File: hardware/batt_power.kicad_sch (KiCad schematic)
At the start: 11 parts, among them J5 JST_PH_01x03, J6 Conn_01x01, J8 Conn_01x01, Q1 AO3400A, U6 TPS7A2030PDBV

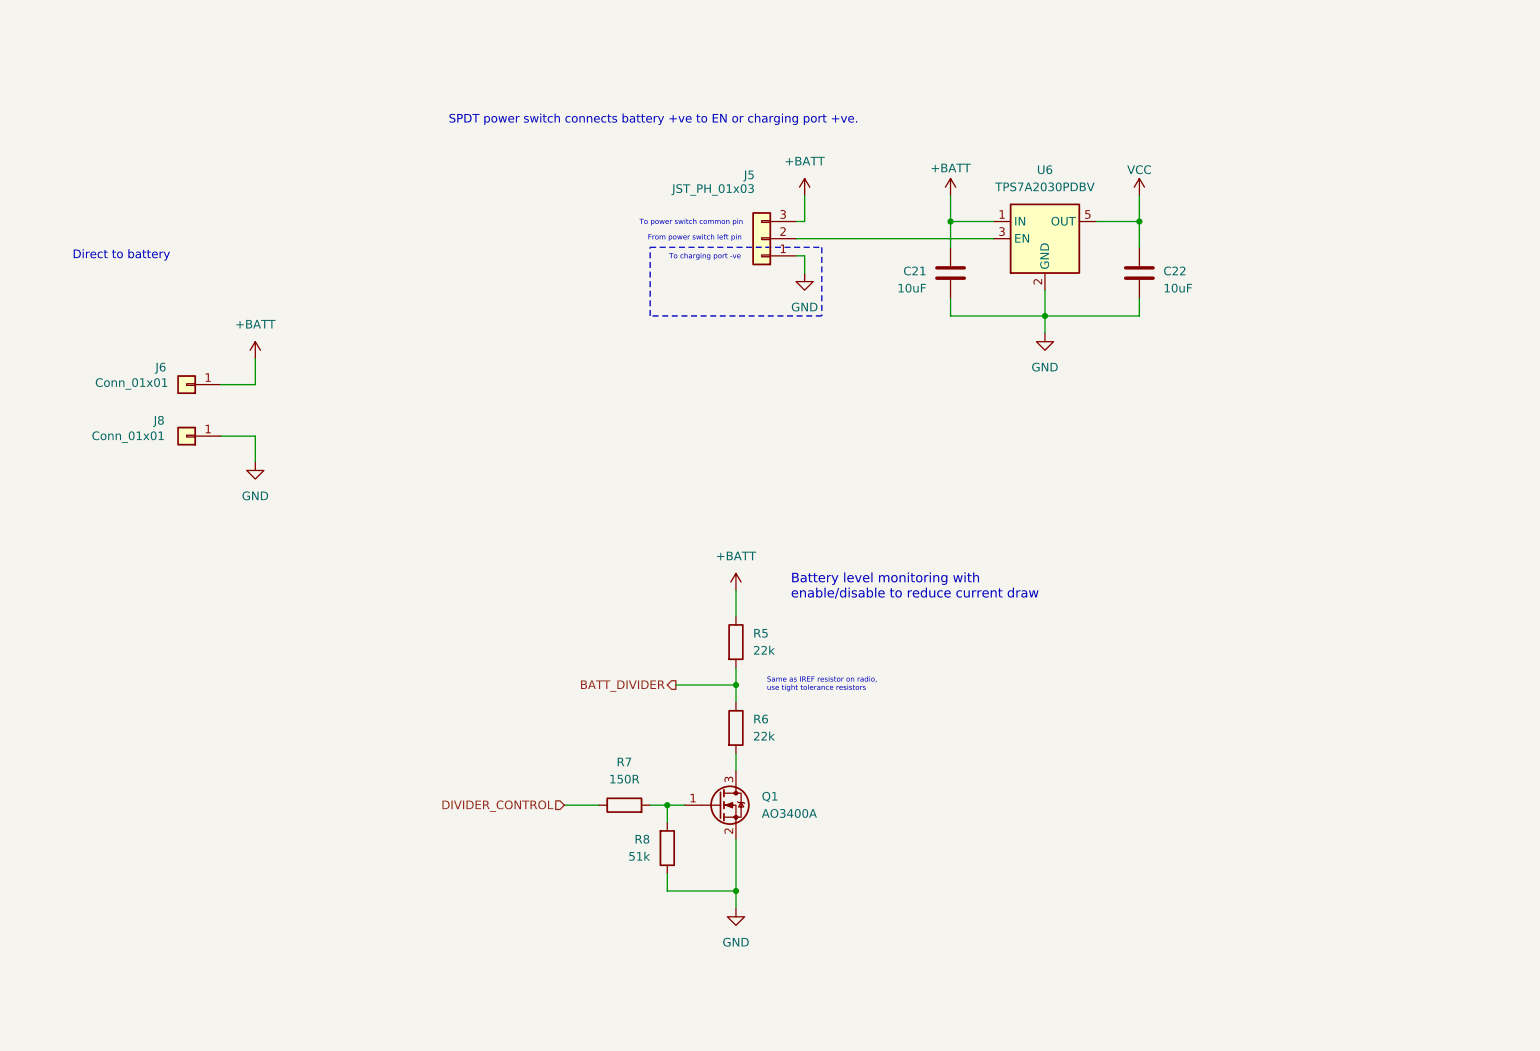
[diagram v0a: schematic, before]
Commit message: Added separate LDO for NRF24
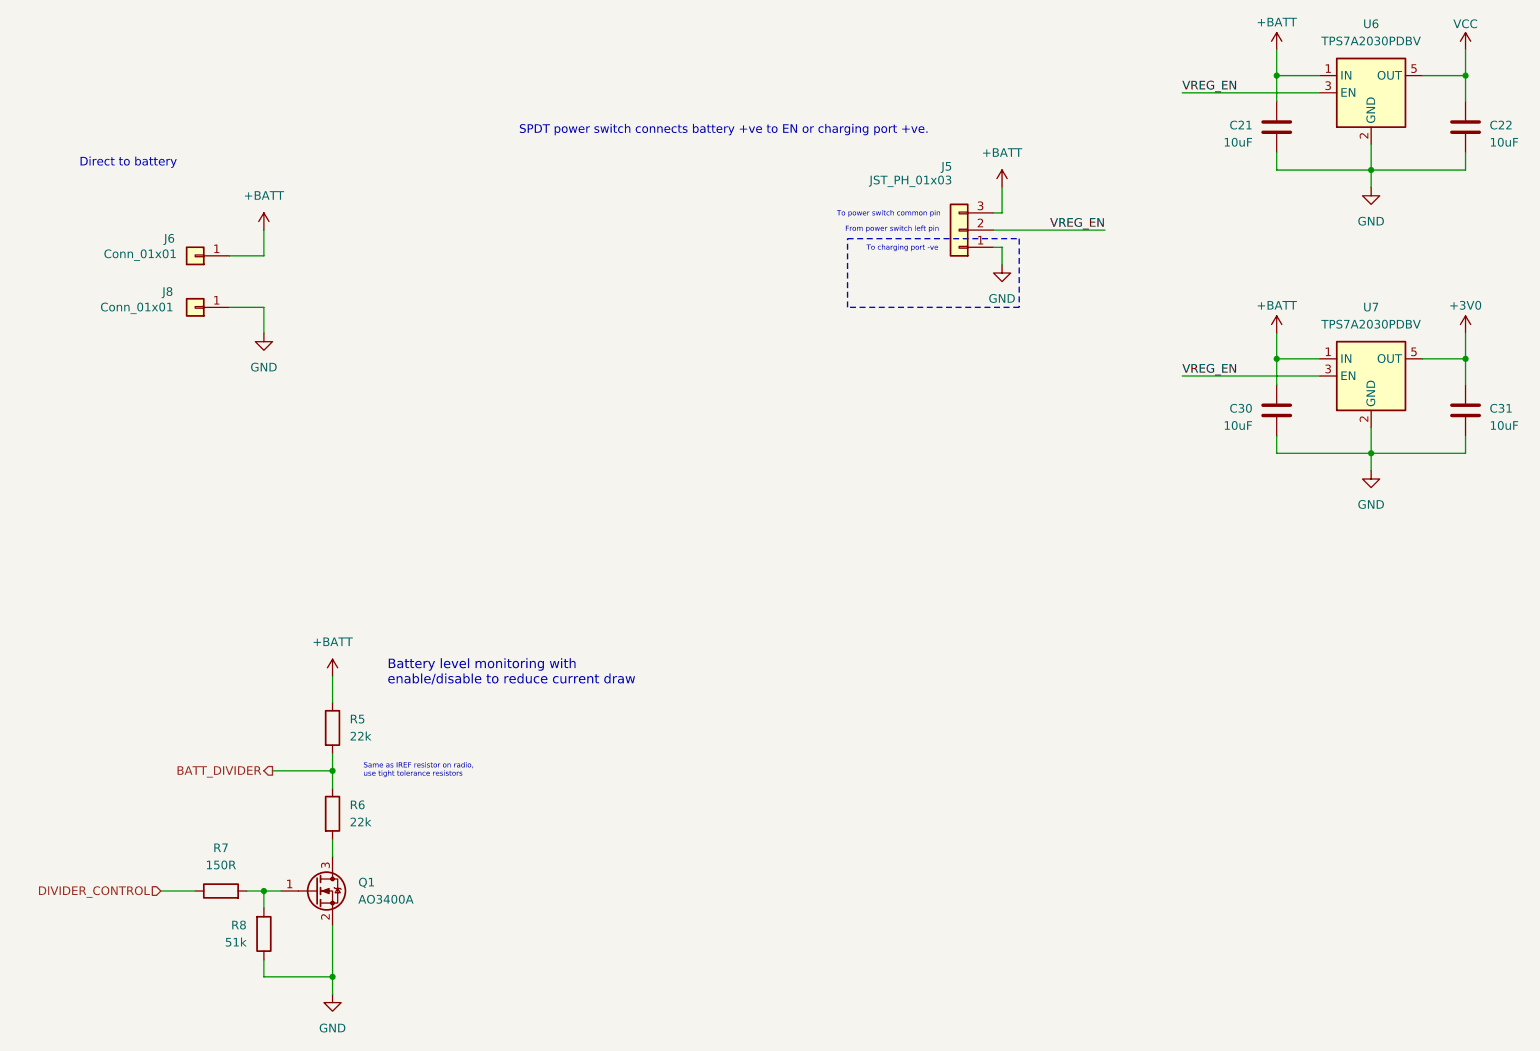
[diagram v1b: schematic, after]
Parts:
- added C30, C31: 10uF, Capacitor_SMD:C_0603_1608Metric_Pad1.08x0.95mm_HandSolder, symbol Device:C
- added U7: TPS7A2030PDBV, Package_TO_SOT_SMD:SOT-23-5_HandSoldering, symbol heli_symbols:TPS7A20
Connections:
- net +BATT: now also C30.1, U7.1 (IN)
- net GND: now also C30.2, C31.2, U7.2 (GND)
- net VREG_EN: now reaches J5.2 (Pin_2), U6.3 (EN)
- net VREG_EN: now also U7.3 (EN)
- new net +3V0: C31.1, U7.5 (OUT)
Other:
- moved on the sheet: C21, C22, J5, J6, J8, Q1, R5, R6, R7, R8, U6

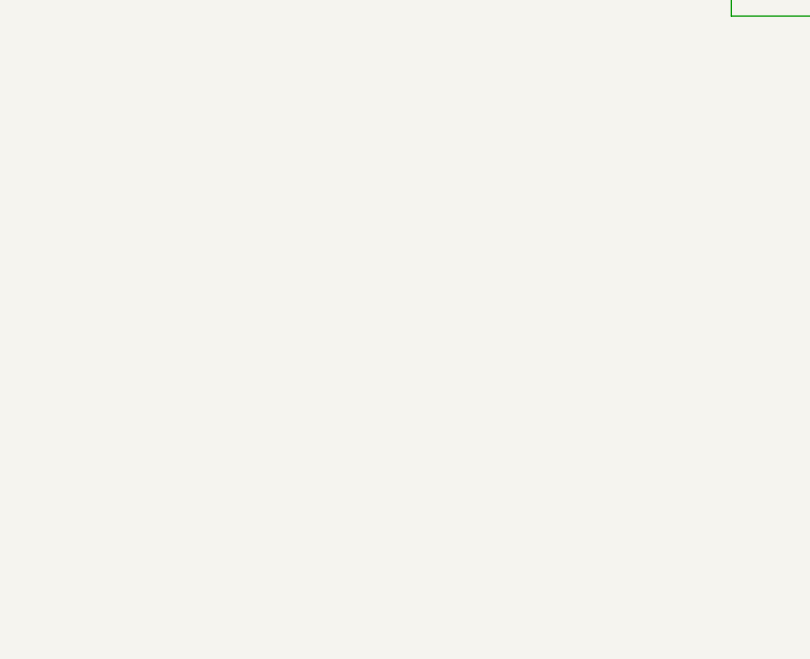
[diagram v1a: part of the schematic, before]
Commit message: Added power testpoints
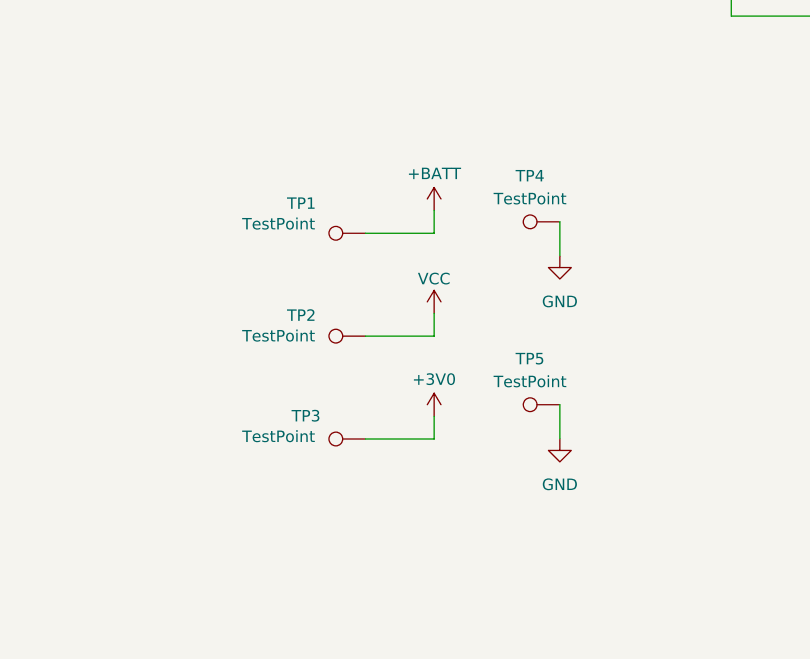
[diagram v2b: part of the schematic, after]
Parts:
- added TP1, TP2, TP3: TestPoint, TestPoint:TestPoint_Pad_1.5x1.5mm, symbol Connector:TestPoint
- added TP4: TestPoint, TestPoint:TestPoint_Pad_D1.5mm, symbol Connector:TestPoint
- added TP5: TestPoint, TestPoint:TestPoint_Keystone_5019_Minature, symbol Connector:TestPoint
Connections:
- net +3V0: now also TP3.1
- net +BATT: now also TP1.1
- net GND: now also TP4.1, TP5.1
- net VCC: now also TP2.1

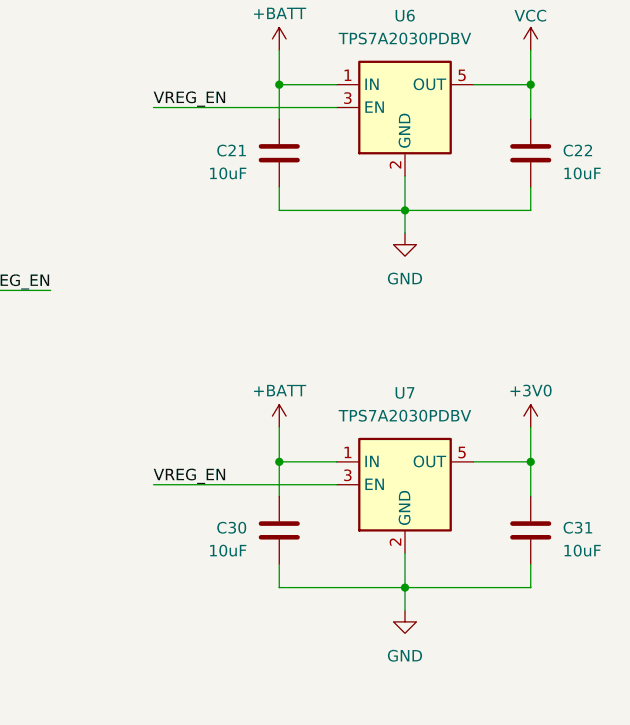
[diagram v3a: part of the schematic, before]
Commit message: Updated VRM capacitor values
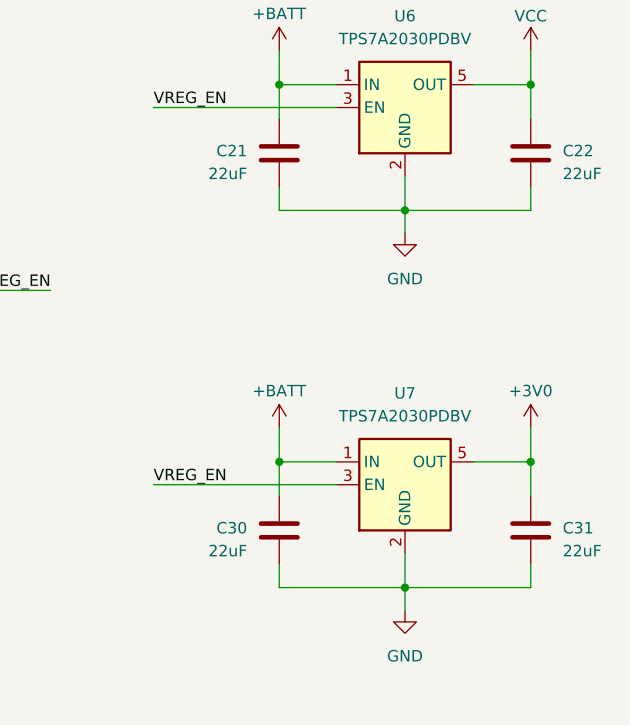
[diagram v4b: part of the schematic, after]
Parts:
- C21, C22, C30, C31: value 10uF -> 22uF
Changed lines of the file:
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@@
 			)
 		)
-		(property "Value" "10uF"
+		(property "Value" "22uF"
 			(at 243.586 44.196 0)
 			(effects
@@
 			)
 		)
-		(property "Value" "10uF"
+		(property "Value" "22uF"
 			(at 243.586 86.106 0)
 			(effects
@@
 			)
 		)
-		(property "Value" "10uF"
+		(property "Value" "22uF"
 			(at 208.534 86.106 0)
 			(effects
@@
 			)
 		)
-		(property "Value" "10uF"
+		(property "Value" "22uF"
 			(at 208.534 44.196 0)
 			(effects

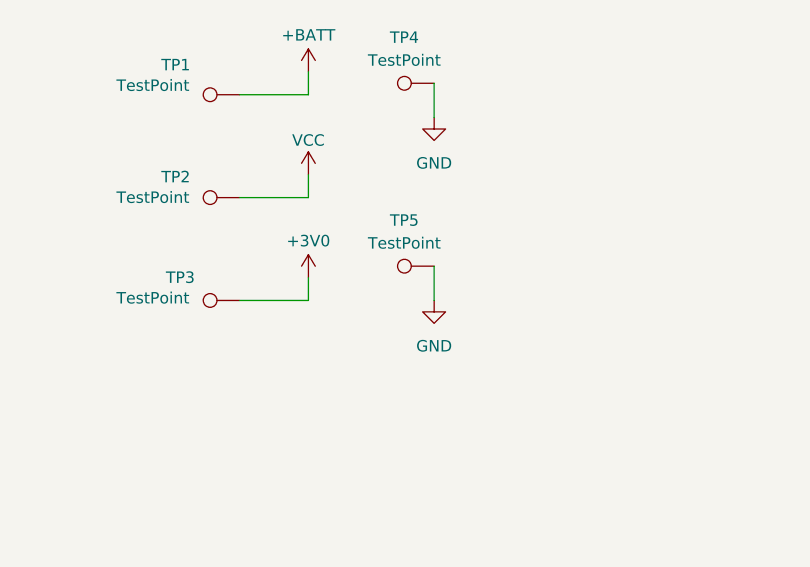
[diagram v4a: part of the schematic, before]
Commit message: Shifted radio components and testpoints around
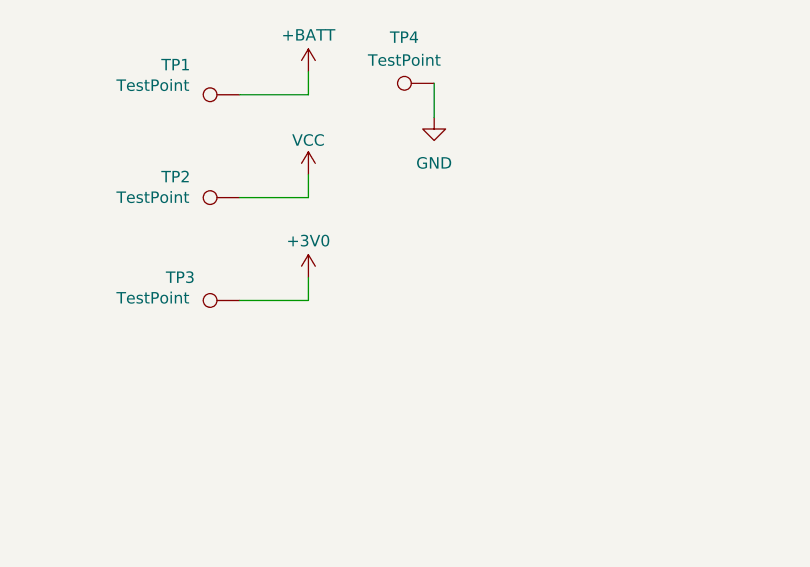
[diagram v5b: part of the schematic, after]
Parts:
- removed TP5: TestPoint, TestPoint:TestPoint_Keystone_5019_Minature, symbol Connector:TestPoint
- TP2: footprint TestPoint:TestPoint_Pad_1.5x1.5mm -> TestPoint:TestPoint_Pad_D1.5mm
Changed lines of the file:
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@@
-	(wire
-		(pts
-			(xy 193.04 133.35) (xy 193.04 137.16)
-		)
-		(stroke
-			(width 0)
-			(type default)
-		)
-	)
 	(wire
 		(pts
@@
 	)
 	(symbol
-		(lib_id "Connector:TestPoint")
-		(at 193.04 133.35 90)
-		(unit 1)
-		(exclude_from_sim no)
-		(in_bom yes)
-		(on_board yes)
-		(dnp no)
-		(fields_autoplaced yes)
-		(property "Reference" "TP5"
-			(at 189.738 128.27 90)
-			(effects
-				(font
-					(size 1.27 1.27)
-				)
-			)
-		)
-		(property "Value" "TestPoint"
-			(at 189.738 130.81 90)
-			(effects
-				(font
-					(size 1.27 1.27)
-				)
-			)
-		)
-		(property "Footprint" "TestPoint:TestPoint_Keystone_5019_Minature"
-			(at 193.04 128.27 0)
-			(effects
-				(font
-					(size 1.27 1.27)
-				)
-				(hide yes)
-			)
-		)
-		(property "Datasheet" "~"
-			(at 193.04 128.27 0)
-			(effects
-				(font
-					(size 1.27 1.27)
-				)
-				(hide yes)
-			)
-		)
-		(property "Description" "test point"
-			(at 193.04 133.35 0)
-			(effects
-				(font
-					(size 1.27 1.27)
-				)
-				(hide yes)
-			)
-		)
-		(pin "1"
-		)
-		(instances
-			(project "heli_avionics"
-				(path "/c384ea46-0dfb-4673-b2f4-1f88fafbcaa5/f8f87cfe-571f-4a92-acee-79776e4ce004"
-					(reference "TP5")
-					(unit 1)
-				)
-			)
-		)
-	)
-	(symbol
 		(lib_id "power:GND")
 		(at 226.06 50.8 0)
@@
 	)
 	(symbol
-		(lib_id "power:GND")
-		(at 193.04 137.16 0)
-		(unit 1)
-		(exclude_from_sim no)
-		(in_bom yes)
-		(on_board yes)
-		(dnp no)
-		(fields_autoplaced yes)
-		(property "Reference" "#PWR062"
-			(at 193.04 143.51 0)
-			(effects
-				(font
-					(size 1.27 1.27)
-				)
-				(hide yes)
-			)
-		)
-		(property "Value" "GND"
-			(at 193.04 142.24 0)
-			(effects
-				(font
-					(size 1.27 1.27)
-				)
-			)
-		)
-		(property "Footprint" ""
-			(at 193.04 137.16 0)
-			(effects
-				(font
-					(size 1.27 1.27)
-				)
-				(hide yes)
-			)
-		)
-		(property "Datasheet" ""
-			(at 193.04 137.16 0)
-			(effects
-				(font
-					(size 1.27 1.27)
-				)
-				(hide yes)
-			)
-		)
-		(property "Description" "Power symbol creates a global label with name \"GND\" , ground"
-			(at 193.04 137.16 0)
-			(effects
-				(font
-					(size 1.27 1.27)
-				)
-				(hide yes)
-			)
-		)
-		(pin "1"
-		)
-		(instances
-			(project "heli_avionics"
-				(path "/c384ea46-0dfb-4673-b2f4-1f88fafbcaa5/f8f87cfe-571f-4a92-acee-79776e4ce004"
-					(reference "#PWR062")
-					(unit 1)
-				)
-			)
-		)
-	)
-	(symbol
 		(lib_id "Device:R")
 		(at 55.88 154.94 90)
@@
 			)
 		)
-		(property "Footprint" "TestPoint:TestPoint_Pad_1.5x1.5mm"
+		(property "Footprint" "TestPoint:TestPoint_Pad_D1.5mm"
 			(at 171.45 120.65 0)
 			(effects

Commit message: Fixed ERC errors
Had to exclude warning for connecting ground to the bidirectional SA0 pin (pin 5) on the pressure sensor.
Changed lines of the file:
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@@
+	)
+	(junction
+		(at 62.23 60.96)
+		(diameter 0)
+		(color 0 0 0 0)
+	)
+	(junction
+		(at 62.23 68.58)
+		(diameter 0)
+		(color 0 0 0 0)
 	)
 	(junction
@@
 	(wire
 		(pts
+			(xy 62.23 68.58) (xy 72.39 68.58)
+		)
+		(stroke
+			(width 0)
+			(type default)
+		)
+	)
+	(wire
+		(pts
 			(xy 72.39 160.02) (xy 72.39 167.64)
 		)
@@
 	(wire
 		(pts
+			(xy 62.23 68.58) (xy 62.23 72.39)
+		)
+		(stroke
+			(width 0)
+			(type default)
+		)
+	)
+	(wire
+		(pts
 			(xy 212.09 45.72) (xy 212.09 48.26)
 		)
@@
 	(wire
 		(pts
+			(xy 72.39 60.96) (xy 62.23 60.96)
+		)
+		(stroke
+			(width 0)
+			(type default)
+		)
+	)
+	(wire
+		(pts
 			(xy 226.06 86.36) (xy 226.06 90.17)
 		)
@@
 	(wire
 		(pts
+			(xy 72.39 57.15) (xy 72.39 60.96)
+		)
+		(stroke
+			(width 0)
+			(type default)
+		)
+	)
+	(wire
+		(pts
 			(xy 62.23 165.1) (xy 62.23 167.64)
 		)
@@
 	(wire
 		(pts
-			(xy 62.23 68.58) (xy 62.23 72.39)
-		)
-		(stroke
-			(width 0)
-			(type default)
-		)
-	)
-	(wire
-		(pts
 			(xy 212.09 30.48) (xy 212.09 34.29)
 		)
@@
 		(pts
 			(xy 212.09 34.29) (xy 218.44 34.29)
+		)
+		(stroke
+			(width 0)
+			(type default)
+		)
+	)
+	(wire
+		(pts
+			(xy 72.39 68.58) (xy 72.39 72.39)
 		)
 		(stroke
@@
 	)
 	(symbol
+		(lib_id "power:PWR_FLAG")
+		(at 72.39 72.39 180)
+		(unit 1)
+		(exclude_from_sim no)
+		(in_bom yes)
+		(on_board yes)
+		(dnp no)
+		(fields_autoplaced yes)
+		(property "Reference" "#FLG02"
+			(at 72.39 74.295 0)
+			(effects
+				(font
+					(size 1.27 1.27)
+				)
+				(hide yes)
+			)
+		)
+		(property "Value" "PWR_FLAG"
+			(at 72.39 77.47 0)
+			(effects
+				(font
+					(size 1.27 1.27)
+				)
+			)
+		)
+		(property "Footprint" ""
+			(at 72.39 72.39 0)
+			(effects
+				(font
+					(size 1.27 1.27)
+				)
+				(hide yes)
+			)
+		)
+		(property "Datasheet" "~"
+			(at 72.39 72.39 0)
+			(effects
+				(font
+					(size 1.27 1.27)
+				)
+				(hide yes)
+			)
+		)
+		(property "Description" "Special symbol for telling ERC where power comes from"
+			(at 72.39 72.39 0)
+			(effects
+				(font
+					(size 1.27 1.27)
+				)
+				(hide yes)
+			)
+		)
+		(pin "1"
+		)
+		(instances
+			(project "heli_avionics"
+				(path "/c384ea46-0dfb-4673-b2f4-1f88fafbcaa5/f8f87cfe-571f-4a92-acee-79776e4ce004"
+					(reference "#FLG02")
+					(unit 1)
+				)
+			)
+		)
+	)
+	(symbol
 		(lib_id "power:GND")
 		(at 226.06 50.8 0)
@@
 					(unit 1)
 				)
+			)
+		)
+	)
+	(symbol
+		(lib_id "power:PWR_FLAG")
+		(at 72.39 57.15 0)
+		(unit 1)
+		(exclude_from_sim no)
+		(in_bom yes)
+		(on_board yes)
+		(dnp no)
+		(fields_autoplaced yes)
+		(property "Reference" "#FLG01"
+			(at 72.39 55.245 0)
+			(effects
+				(font
+					(size 1.27 1.27)
+				)
+				(hide yes)
+			)
+		)
+		(property "Value" "PWR_FLAG"
+			(at 72.39 52.07 0)
+			(effects
+				(font
+					(size 1.27 1.27)
+				)
+			)
+		)
+		(property "Footprint" ""
+			(at 72.39 57.15 0)
+			(effects
+				(font
+					(size 1.27 1.27)
+				)
+				(hide yes)
+			)
+		)
+		(property "Datasheet" "~"
+			(at 72.39 57.15 0)
+			(effects
+				(font
+					(size 1.27 1.27)
+				)
+				(hide yes)
+			)
+		)
+		(property "Description" "Special symbol for telling ERC where power comes from"
+			(at 72.39 57.15 0)
+			(effects
+				(font
+					(size 1.27 1.27)
+				)
+				(hide yes)
+			)
+		)
+		(pin "1"
+		)
+		(instances
+			(project ""
+				(path "/c384ea46-0dfb-4673-b2f4-1f88fafbcaa5/f8f87cfe-571f-4a92-acee-79776e4ce004"
+					(reference "#FLG01")
+					(unit 1)
+				)
